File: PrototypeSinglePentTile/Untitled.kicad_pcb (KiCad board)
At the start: 2 copper layers, 30.7 x 32.3 mm, 12 parts

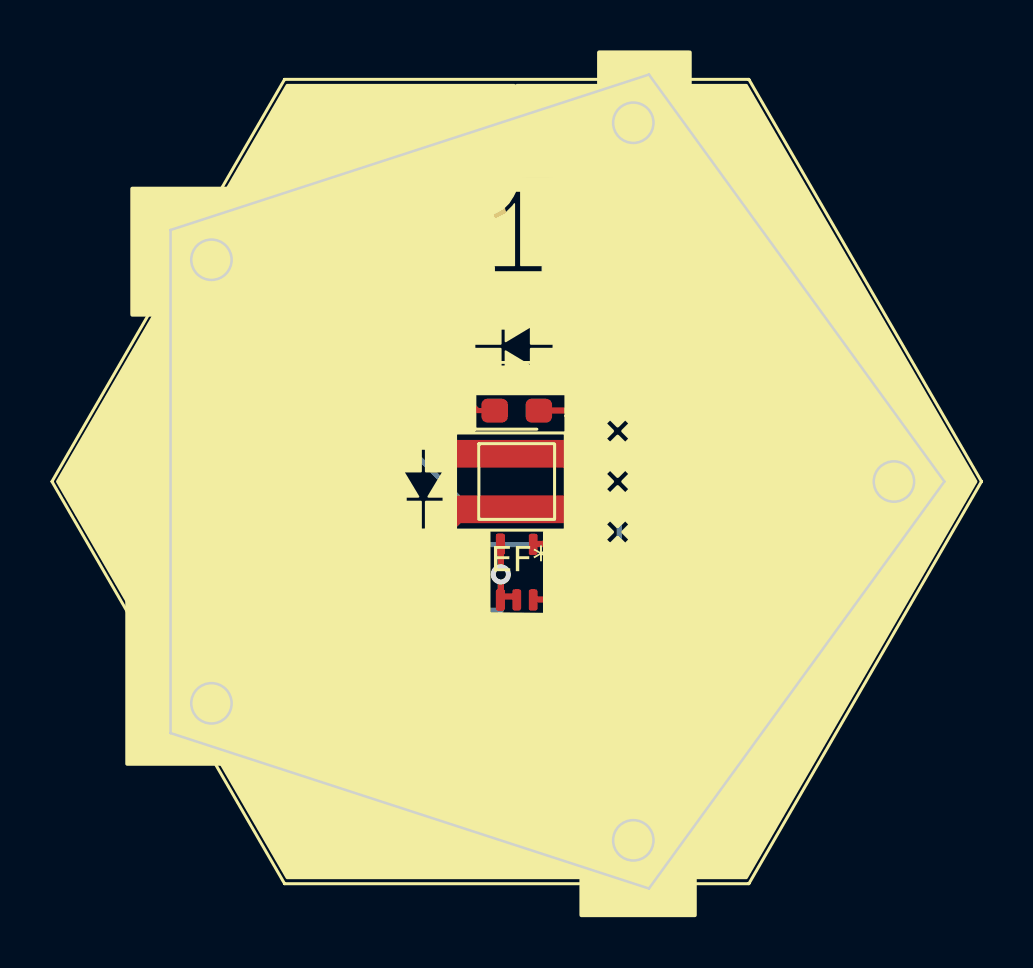
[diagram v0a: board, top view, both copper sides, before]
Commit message: v5 of the prototype hexboard and squareboards:  added label to capacitors and resistors; moved temperature sensors to periphery; added 0.1 mm back to top and bottom of boards
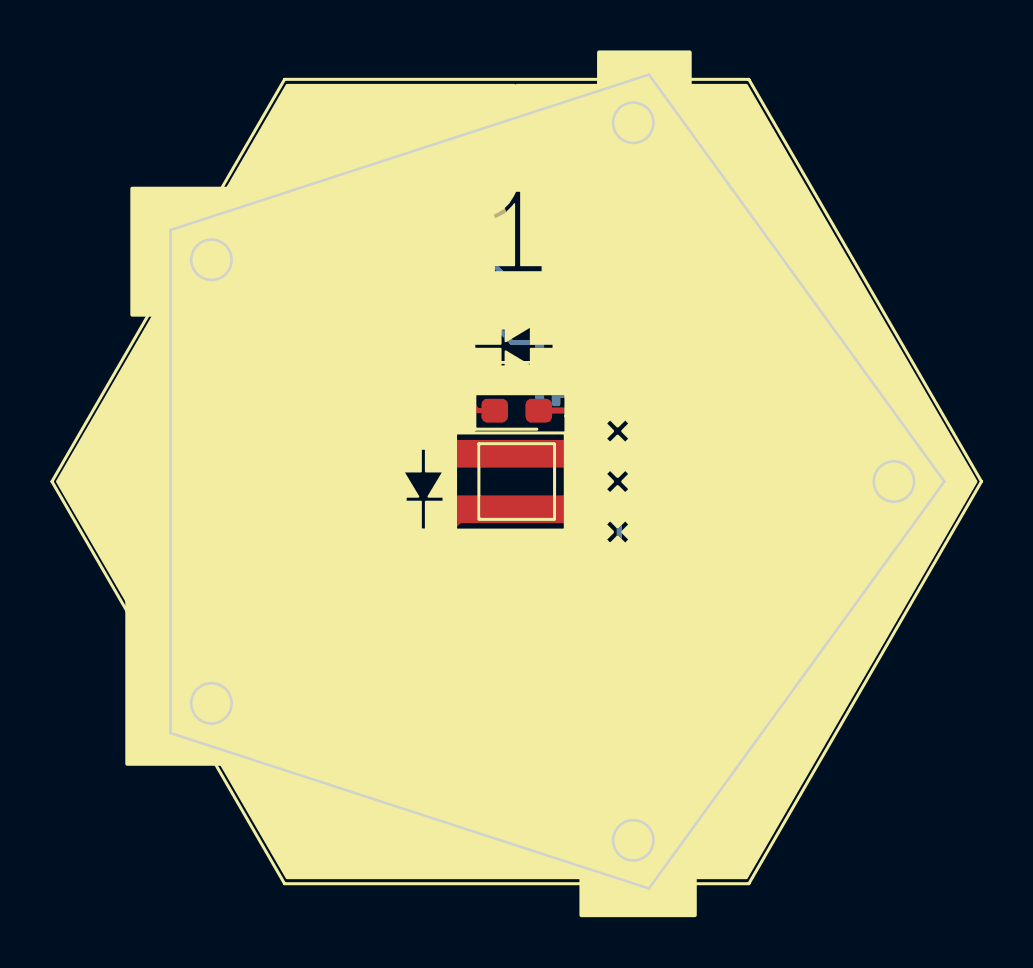
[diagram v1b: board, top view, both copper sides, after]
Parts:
- removed ? (x2): , 
- REF**: moved to B.Cu
- REF**: value R_0402_1005Metric -> R_1206_3216Metric; footprint Resistor_SMD:R_0402_1005Metric -> Resistor_SMD:R_1206_3216Metric
- moved REF** 8.25 mm to (105.3, 53.5), turned to 180 degrees
- moved REF** 2.10 mm to (110.1, 62.9)
- moved G*** 0.78 mm to (113.6, 65.0), turned to -118 degrees
- moved REF** 0.72 mm to (113.2, 58.2)
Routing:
- net (no net): track 184.1 -> 153.1 mm, vias 4 -> 1
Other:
- board text added: "Designed by Sebouh J. Paul v2 sidelength=19.93 mm"
- board text removed: "Designed by Sebouh J. Paul v1 sidelength=19.93 mm"
